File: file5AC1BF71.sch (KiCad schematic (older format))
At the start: 35 parts

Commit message: Board Layout redesign
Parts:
- added JTP1: TEST_1P, Measurement_Points:Measurement_Point_Round-SMD-Pad_Small, symbol TEST_1P
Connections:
- wire segments 171 -> 172
- no-connect marks 7 -> 6
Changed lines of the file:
@@
 Text Label 3975 3175 0    60   ~ 0
 VCORETURN
-NoConn ~ 5900 3675
 NoConn ~ 5900 3175
 NoConn ~ 5900 3775
@@
 	1    0    0    -1
 $EndComp
+Wire Wire Line
+	5900 3675 6025 3675
+$Comp
+L TEST_1P JTP1
+U 1 1 5AEB993D
+P 6025 3675
+F 0 "JTP1" V 5925 3800 50  0000 C CNN
+F 1 "TEST_1P" H 6025 3875 50  0001 C CNN
+F 2 "Measurement_Points:Measurement_Point_Round-SMD-Pad_Small" H 6225 3675 50  0001 C CNN
+F 3 "" H 6225 3675 50  0001 C CNN
+	1    6025 3675
+	0    1    1    0
+$EndComp
 $EndSCHEMATC

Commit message: Layout updates
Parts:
- added R_SFOUT1: 100K, Resistors_SMD:R_0805_HandSoldering, symbol R
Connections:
- wire segments 172 -> 176
- no-connect marks 6 -> 4
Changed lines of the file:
@@
 VCORETURN
 NoConn ~ 5900 3175
-NoConn ~ 5900 3775
 NoConn ~ 4500 3775
 $Comp
@@
 	1    0    0    -1
 $EndComp
-NoConn ~ 5900 3875
 $Comp
 L NPOT SWING1
@@
 	0    1    1    0
 $EndComp
+Wire Wire Line
+	5900 3875 5950 3875
+Text HLabel 5950 3875 2    60   Input ~ 0
+9V
+$Comp
+L R R_SFOUT1
+U 1 1 5AEE652B
+P 6275 4000
+F 0 "R_SFOUT1" V 6355 4000 50  0000 C CNN
+F 1 "100K" V 6275 4000 50  0000 C CNN
+F 2 "Resistors_SMD:R_0805_HandSoldering" V 6205 4000 50  0001 C CNN
+F 3 "" H 6275 4000 50  0001 C CNN
+	1    6275 4000
+	1    0    0    -1
+$EndComp
+Wire Wire Line
+	5900 3775 6275 3775
+Wire Wire Line
+	6275 3775 6275 3850
+Wire Wire Line
+	6275 4150 6275 4300
+Text Label 6275 4300 1    39   ~ 0
+GND
 $EndSCHEMATC

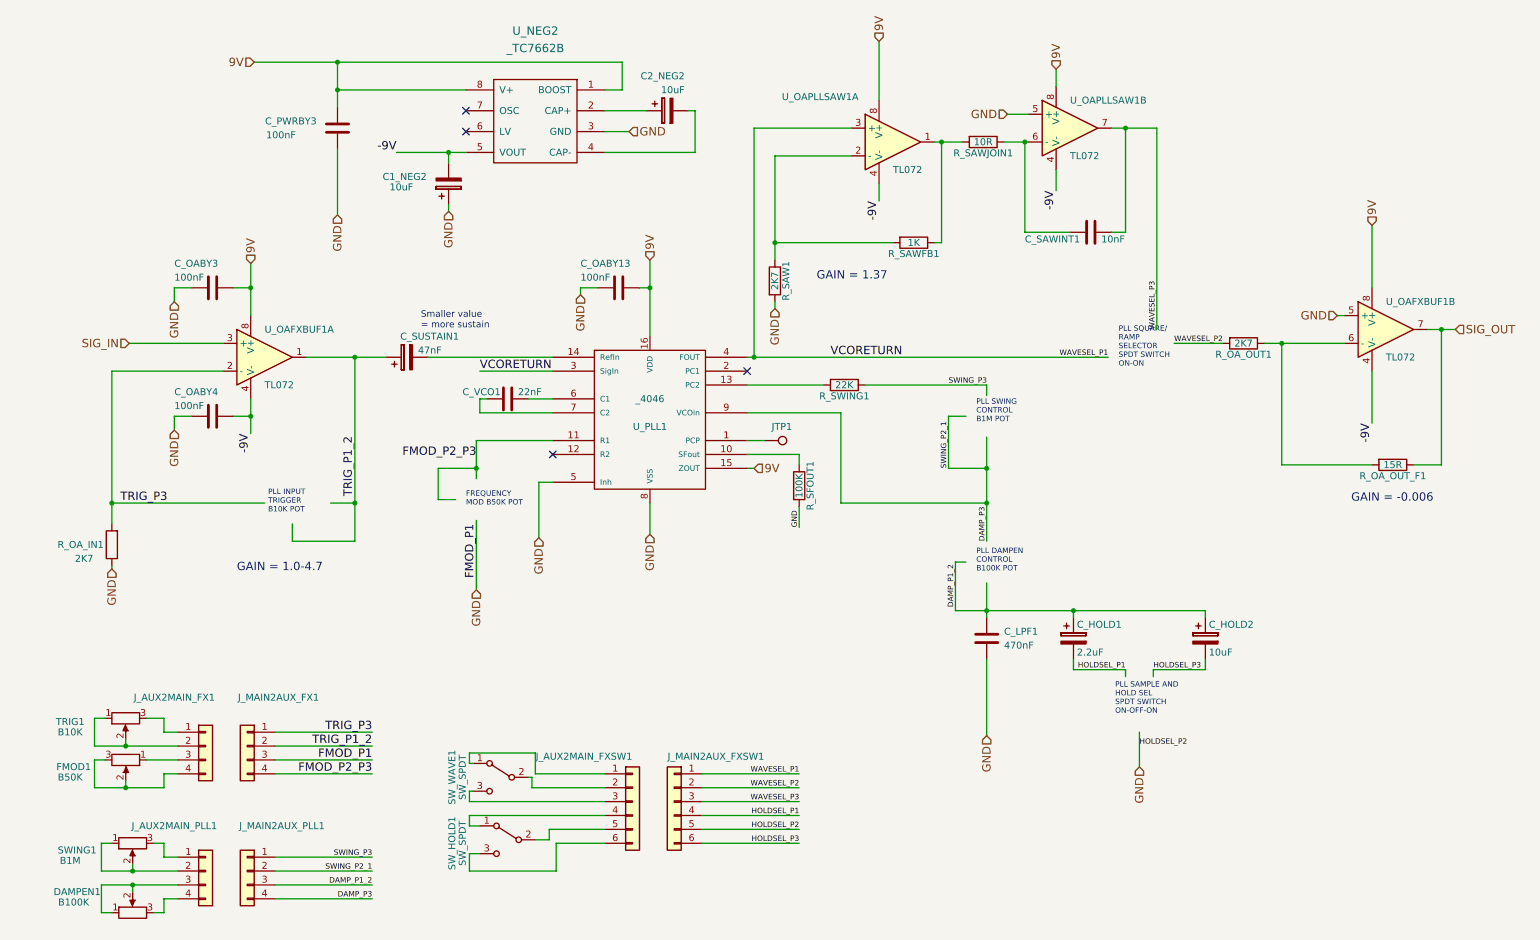
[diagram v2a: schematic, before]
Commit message: Board Redesign - RevB
- Created seperate ground plane for DC-DC Converters
- Re-routed the rest of the board.
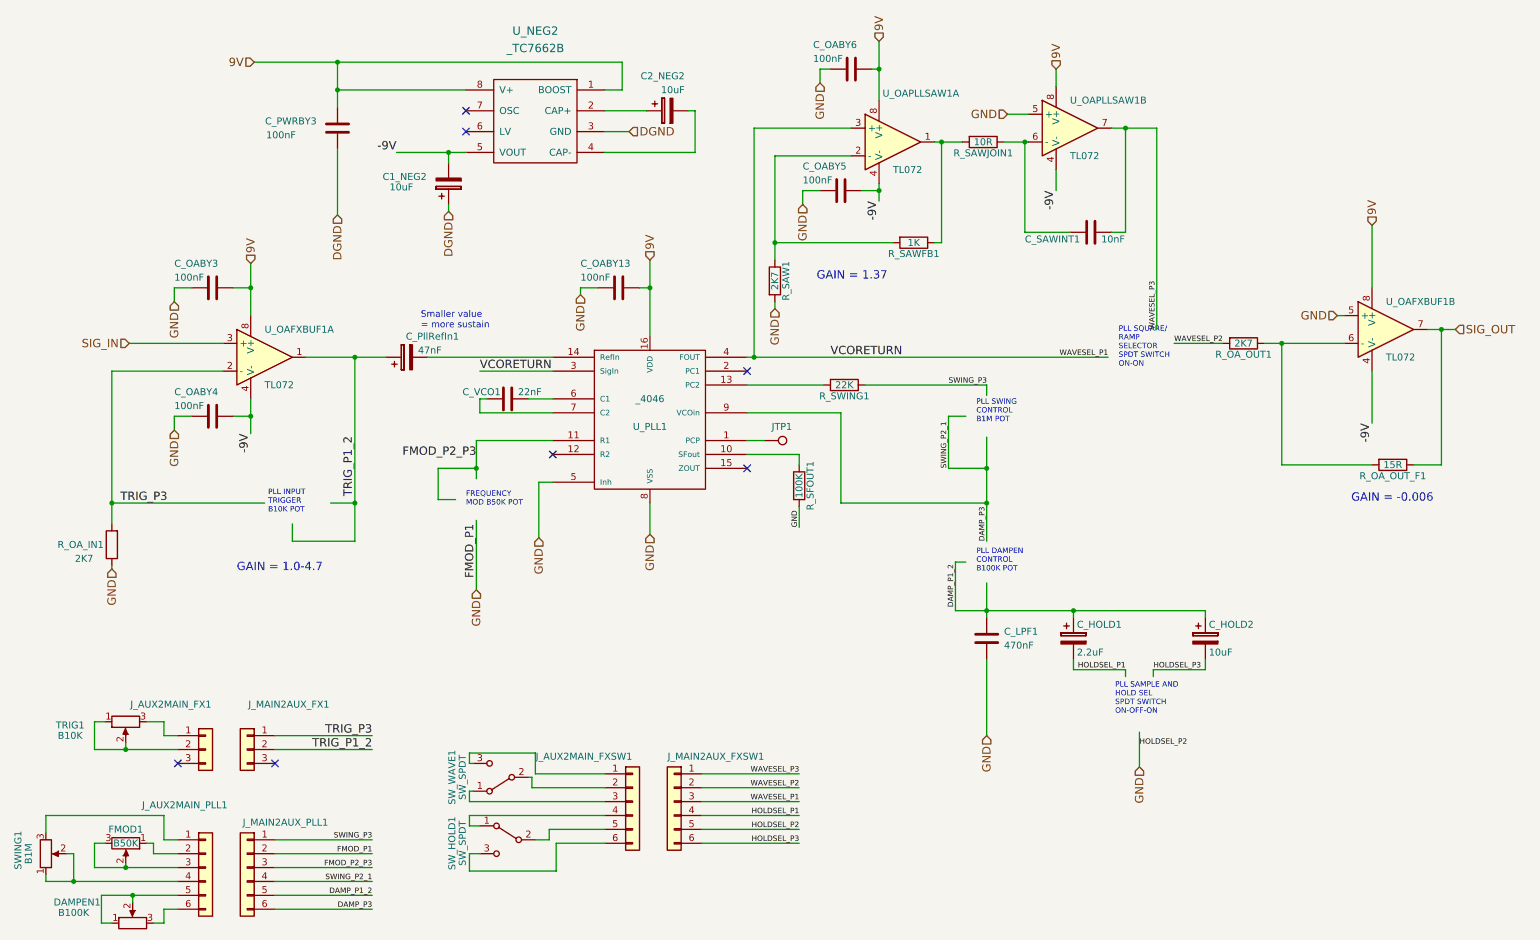
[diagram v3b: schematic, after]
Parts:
- removed J_AUX2MAIN_FX1, J_AUX2MAIN_PLL1, J_MAIN2AUX_FX1, J_MAIN2AUX_PLL1: Conn_01x04, Pin_Headers:Pin_Header_Straight_1x04_Pitch2.54mm, symbol Conn_01x04
- added C_OABY5, C_OABY6: 100nF, Capacitors_SMD:C_0805_HandSoldering, symbol C
- added J_AUX2MAIN_FX1, J_MAIN2AUX_FX1: Conn_01x03, Pin_Headers:Pin_Header_Straight_1x03_Pitch2.54mm, symbol Conn_01x03
- added J_AUX2MAIN_PLL1, J_MAIN2AUX_PLL1: Conn_01x06, Pin_Headers:Pin_Header_Straight_1x06_Pitch2.54mm, symbol Conn_01x06
- renumbered C_SUSTAIN1 to C_PllRefIn1
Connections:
- net labels added: DGND
- wire segments 176 -> 182
- no-connect marks 4 -> 7
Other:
- moved on the sheet: DAMPEN1, FMOD1, SWING1, TRIG1
